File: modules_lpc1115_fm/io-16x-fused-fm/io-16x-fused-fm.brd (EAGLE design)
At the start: 48.8 x 50.7 mm, 144 parts, among them IC5 LPC1115, IC6 ATAES132A-SHEQ-T, J1 62000611622, J2 1771017, J3 1770953, Q3 ASFL, U3 EEPROM, X1 MICROMATCH-10SMD

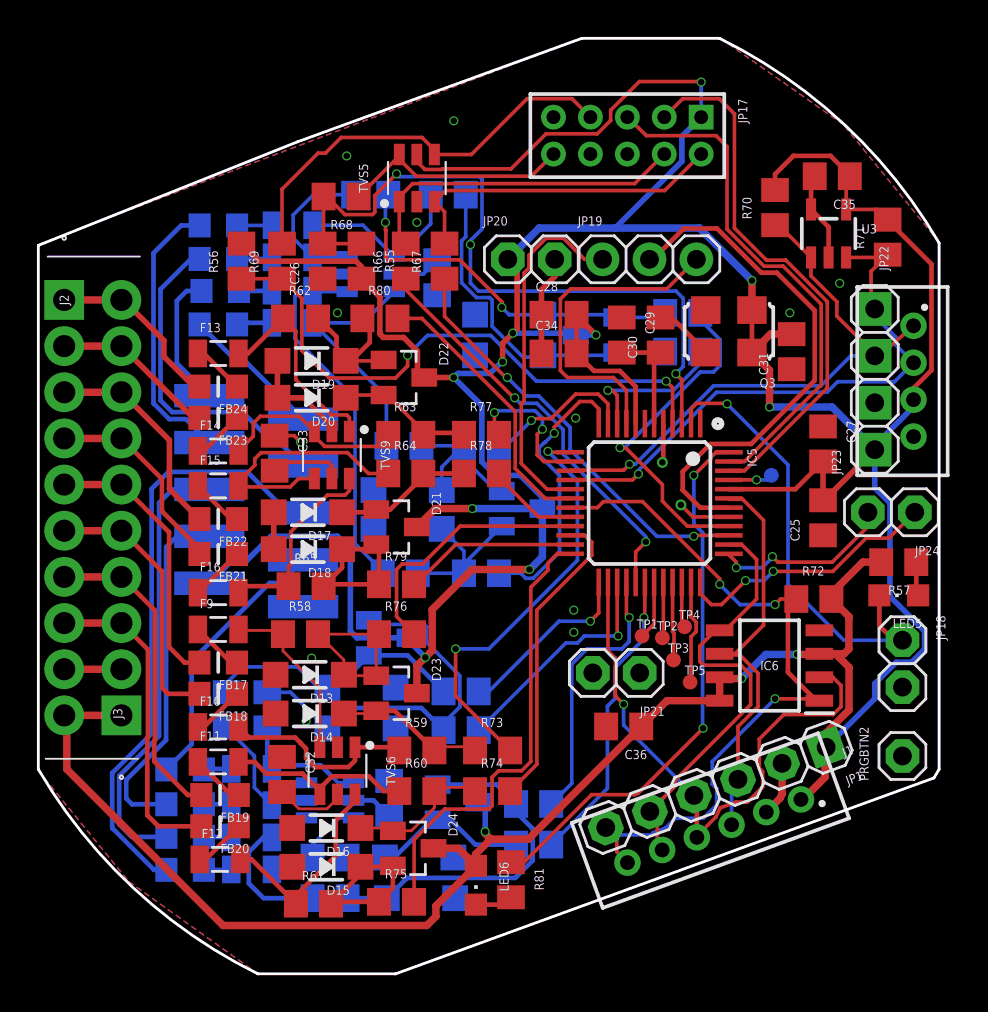
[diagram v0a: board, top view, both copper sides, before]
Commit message: [IO16xFM] - new branch for designing a slightly smaller BRD
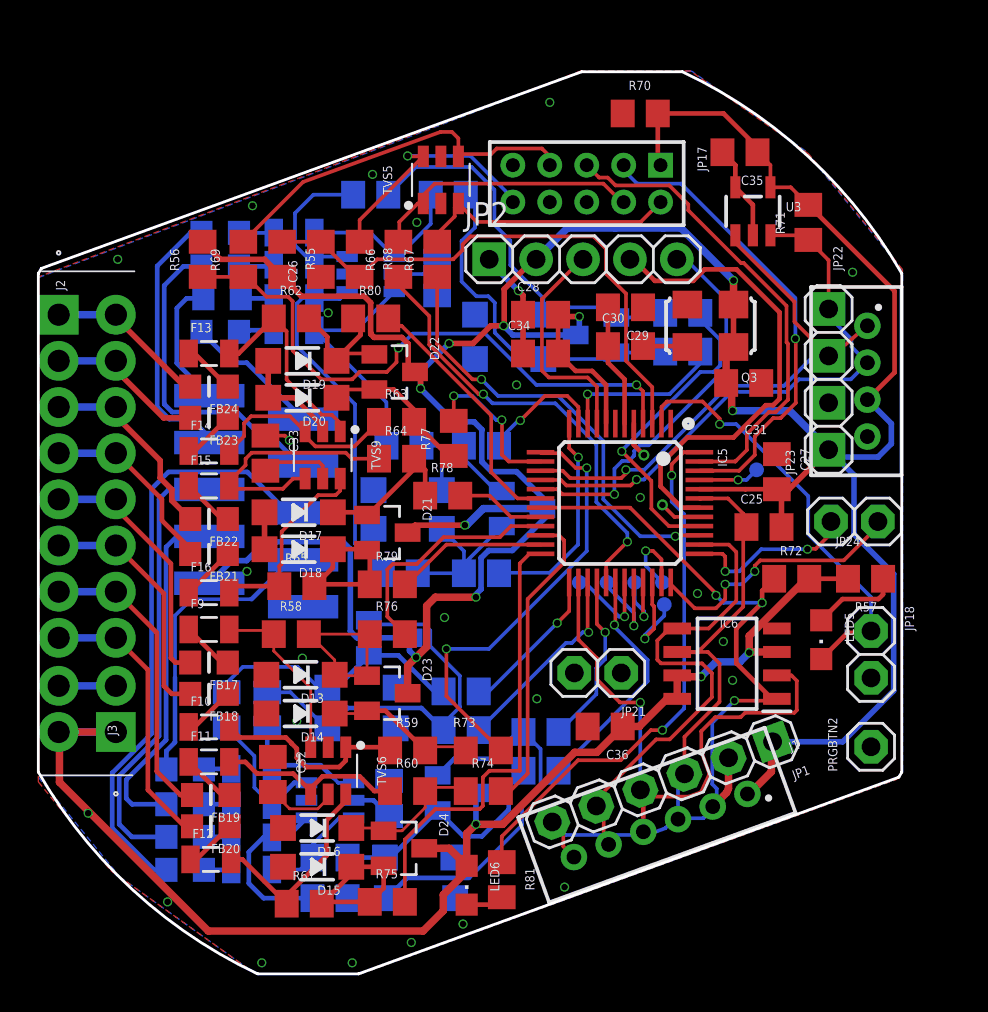
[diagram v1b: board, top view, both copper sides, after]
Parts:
- removed JP19: (no value), pinhead_dmx:1X03
- removed JP20: (no value), pinhead_dmx:1X02
- added JP2: (no value), pinhead_dmx:1X05
- moved R70 8.91 mm to (32.6, 46.6), turned to 0 degrees
- moved TP5 5.60 mm to (33.8, 21.2), flipped to the bottom
- moved C35 5.17 mm to (38.0, 44.5)
- moved LED5 4.84 mm to (42.4, 18.1), turned to 180 degrees
- moved TP3 4.70 mm to (32.3, 21.2), flipped to the bottom
- moved TP1 4.47 mm to (29.3, 21.2), flipped to the bottom
- moved R71 4.37 mm to (41.7, 40.7)
- moved R55 4.30 mm to (13.2, 38.7)
- moved U3 4.27 mm to (38.7, 41.3)
- moved TP2 4.24 mm to (30.8, 21.2), flipped to the bottom
- moved R10 4.02 mm to (27.2, 11.0)
- moved R11 3.92 mm to (27.2, 13.1)
- moved R68 3.54 mm to (17.4, 38.7), turned to 270 degrees
- moved JP17 3.41 mm to (29.7, 42.8)
- moved C25 3.24 mm to (39.3, 24.2), turned to 0 degrees
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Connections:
- net +3V3: now also JP2.2; no longer JP20.1
- net BUS_V: now also JP2.4; no longer JP19.2
- net EIB_IN: now also JP2.3; no longer JP19.3
- net EIB_OUT: now also JP2.5; no longer JP19.1
- net GND: now also JP2.1; no longer JP20.2
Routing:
- net +3V3: track 289.7 -> 260.7 mm, vias 13 -> 12
- net RESET: track 40.1 -> 30.2 mm, vias 3 -> 0
- net EIB_IN: track 18.0 -> 12.3 mm
- net IO12: track 14.9 -> 9.33 mm
- net N$58: track 19.0 -> 23.3 mm
- net IO16: track 15.5 -> 11.7 mm
- net SWD_SWDIO: track 18.0 -> 14.4 mm
- net IO11: track 16.3 -> 13.0 mm
- net SWD_SWCLK: track 18.0 -> 14.8 mm
- net N$60: track 2.46 -> 5.58 mm, vias 0 -> 1
- net ISP_RXD: track 29.3 -> 26.2 mm, vias 0 -> 1
- net SSEL1: track 40.5 -> 43.4 mm
- net N$26: track 1.84 -> 4.78 mm
- net N$57: track 10.5 -> 13.4 mm
- net MOSI1: track 24.0 -> 26.8 mm
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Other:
- board size 48.8 x 50.7 mm -> 46.8 x 48.9 mm
- board text added: "GND 3V3"
- board text added: "IO1 IO2 ... IO8"
- board text added: "www.selfbus.org IO module 16x fused alpha1"

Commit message: [IO16xFM] - eliminated all DRC errors
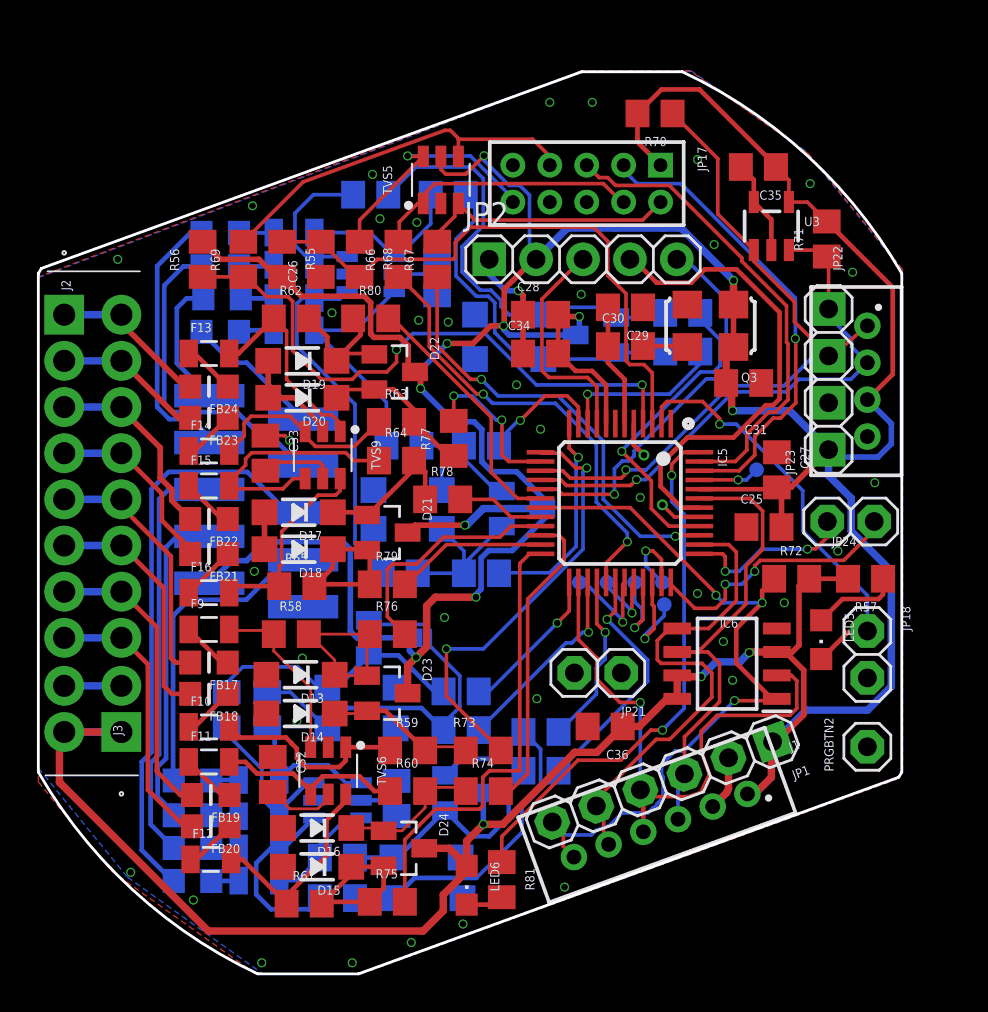
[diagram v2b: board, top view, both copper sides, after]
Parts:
- moved R71 1.35 mm to (42.7, 39.8)
- moved C35 1.28 mm to (39.0, 43.7)
- moved U3 1.28 mm to (39.7, 40.5)
- moved R70 0.80 mm to (33.4, 46.6), turned to 180 degrees
- moved F2 0.72 mm to (11.9, 8.54)
- moved FB3 0.72 mm to (8.35, 5.03)
- moved FB1 0.72 mm to (8.35, 10.5)
- moved FB2 0.72 mm to (8.35, 8.59)
- moved FB4 0.72 mm to (8.35, 6.82)
- moved F1 0.72 mm to (11.9, 10.5)
- moved F3 0.72 mm to (11.9, 5.05)
- moved F4 0.72 mm to (11.9, 6.79)
- moved D3 0.40 mm to (21.0, 6.30)
- moved C1 0.40 mm to (19.4, 9.50)
- moved D4 0.40 mm to (21.1, 4.10)
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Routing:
- net +3V3: track 260.7 -> 280.5 mm, vias 12 -> 13
- net SCL: track 29.9 -> 37.9 mm
- net N$18: track 21.8 -> 24.2 mm
- net SSEL1: track 43.4 -> 41.6 mm
- net N$24: track 24.3 -> 22.5 mm
- net N$22: track 19.4 -> 17.7 mm
- net SCK1: track 24.3 -> 25.8 mm
- net N$46: track 3.93 -> 5.42 mm
- net RESET: track 30.2 -> 31.7 mm
- net N$27: track 5.30 -> 3.90 mm
- net N$58: track 23.3 -> 22.0 mm
- net SDA: track 30.7 -> 29.4 mm
- net N$53: track 7.60 -> 8.79 mm
- net N$54: track 7.26 -> 8.27 mm
- net N$23: track 32.6 -> 31.7 mm
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
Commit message: [IO16xFM] - rearranged I2C and SPI connectors
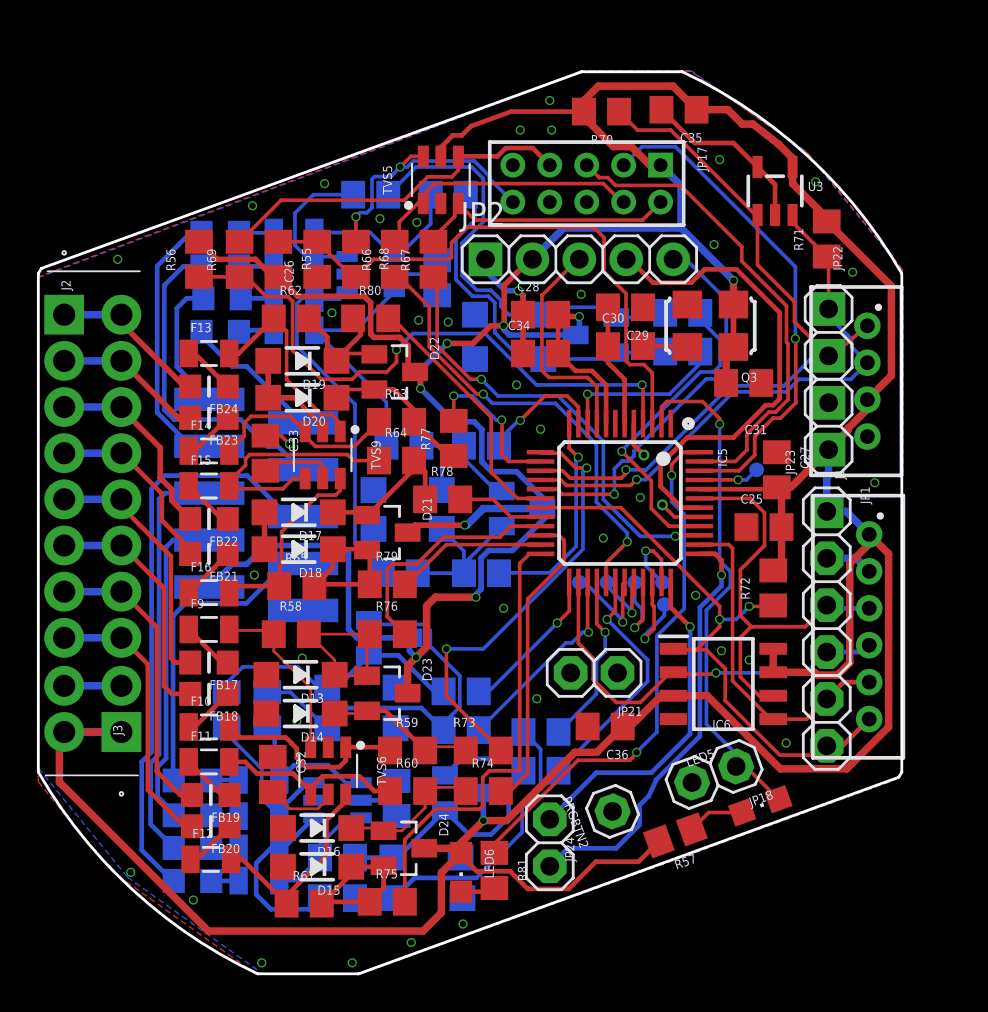
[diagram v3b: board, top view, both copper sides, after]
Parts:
- moved JP24 23.8 mm to (27.7, 7.10), turned to 270 degrees
- moved R57 17.3 mm to (34.5, 7.50), turned to 200 degrees
- moved J1 14.9 mm to (44.4, 18.8), turned to 90 degrees
- moved PRGBTN2 14.2 mm to (31.1, 8.80), turned to 110 degrees
- moved JP1 12.2 mm to (42.7, 18.7), turned to 270 degrees
- moved JP18 10.5 mm to (36.6, 10.8), turned to 200 degrees
- moved LED5 9.59 mm to (39.1, 9.10), turned to 290 degrees
- moved C35 5.30 mm to (34.7, 46.8)
- moved R70 2.90 mm to (30.5, 46.7)
- moved U3 1.91 mm to (39.9, 42.4)
- moved IC6 1.12 mm to (37.1, 15.7), turned to 0 degrees
- moved R72 1.12 mm to (39.8, 20.9), turned to 90 degrees
- moved LED6 0.76 mm to (22.9, 5.50)
- moved R81 0.64 mm to (24.7, 5.60)
- moved R67 0.20 mm to (21.4, 38.7)
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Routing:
- net DBG_RXD: track 9.42 -> 23.2 mm, vias 2 -> 1
- net +3V3: track 280.5 -> 289.4 mm, vias 13 -> 9
- net MOSI1: track 26.8 -> 18.2 mm
- net MISO1: track 30.9 -> 22.4 mm
- net SSEL1: track 41.6 -> 33.8 mm, vias 3 -> 2
- net PROG: track 23.0 -> 27.9 mm
- net GND: track 31.0 -> 35.1 mm
- net DBG_TXD: track 14.5 -> 18.2 mm, vias 2 -> 1
- net SCK1: track 25.8 -> 22.9 mm
- net SCL: track 37.9 -> 40.3 mm
- net N$26: track 4.78 -> 3.10 mm
- net ISP_RXD: track 25.5 -> 27.1 mm
- net SDA: track 29.4 -> 30.3 mm
- net SWD_RESET: track 13.8 -> 14.5 mm, vias 1 -> 2
- net SWD_ISP_EN: track 20.4 -> 19.7 mm
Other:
- board text added: "www.selfbus.org IO module 16x fused beta"
- board text removed: "www.selfbus.org IO module 16x fused alpha1"
